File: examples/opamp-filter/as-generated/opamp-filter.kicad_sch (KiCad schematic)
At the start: 22 parts, among them J1 IN, J2 5V, J3 OUT, U1 MCP6001R, U2 MCP6001R

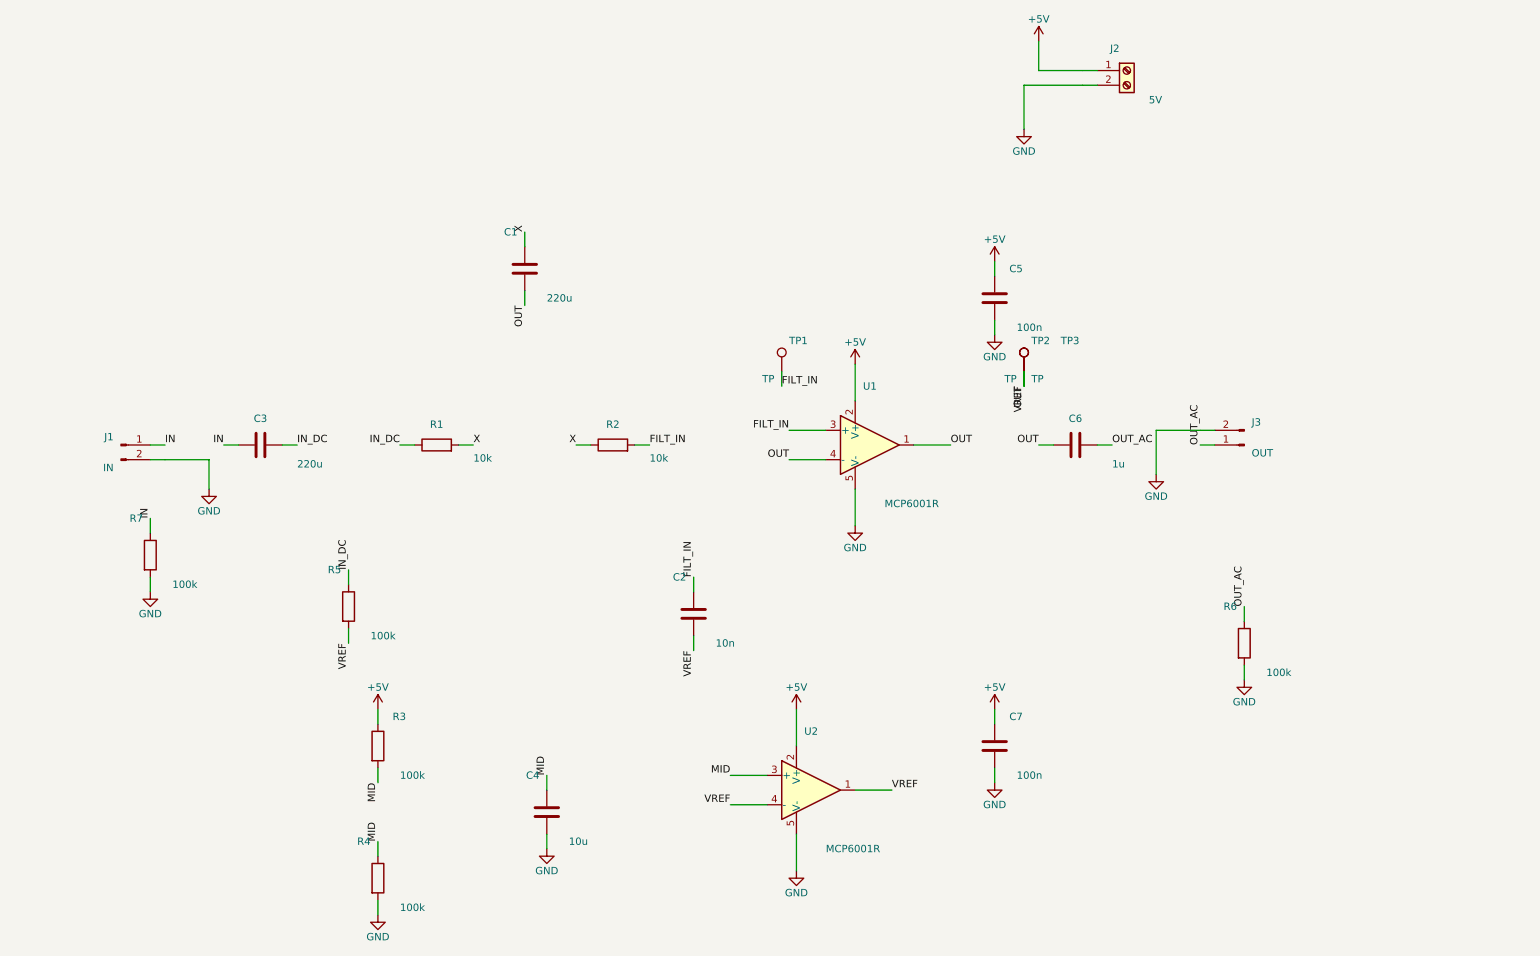
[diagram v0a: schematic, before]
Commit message: Relieve the pads, fillet the joints, and give the board its screw holes
Three of the reviewer's manufacturing points, and they largely fall out
of the one before it - once KiCad fills the plane, the thermal relief it
was already asked for in the file actually appears.

**Thermal relief.** The zones said thermal all along; our own filler
ignored it and flooded every land solid. KiCad's does not, so every
through-hole ground pad now sits in a gap bridged by four spokes and an
iron can bring the joint up without heating a hundred square millimetres
of copper. `layout.solid_pad_connection` reports the setting when a
board turns it off: drilled pads only, because a surface pad reflows in
an oven that is heating the plane anyway and flooding it is often the
better thermal answer.

**Teardrops.** A track entering a land is a step change in width, and a
step change is where copper tears - the connector gets levered on and
off, the drill wanders, and the crack starts at the corner. `_teardrops`
replaces the first stretch of each run with a three-step taper into the
land, checked against its neighbours before it is kept, so a fillet
never eats the clearance a fine-pitch escape needs. It *replaces* rather
than overlays: laying the taper on top of the run drew the same copper
twice, and `route.acute_angle` reported all thirty of them, correctly.
`route.mixed_track_widths` learns what a fillet looks like so a properly
filleted board does not read as one nobody decided the width of.

**Mounting holes.** Four M3 holes near the corners, placed before the
router runs because they are obstacles, and slid along the edges or a
little inboard where a connector body has the corner - the motor board
and the op-amp take three, which is what those floorplans have room for.
Grounded on the motor driver, whose chassis is metal and part of the
shield, plain on the rest: bonding the enclosure to the reference is the
enclosure's decision, not the board's.

Two things that fell out of placing par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
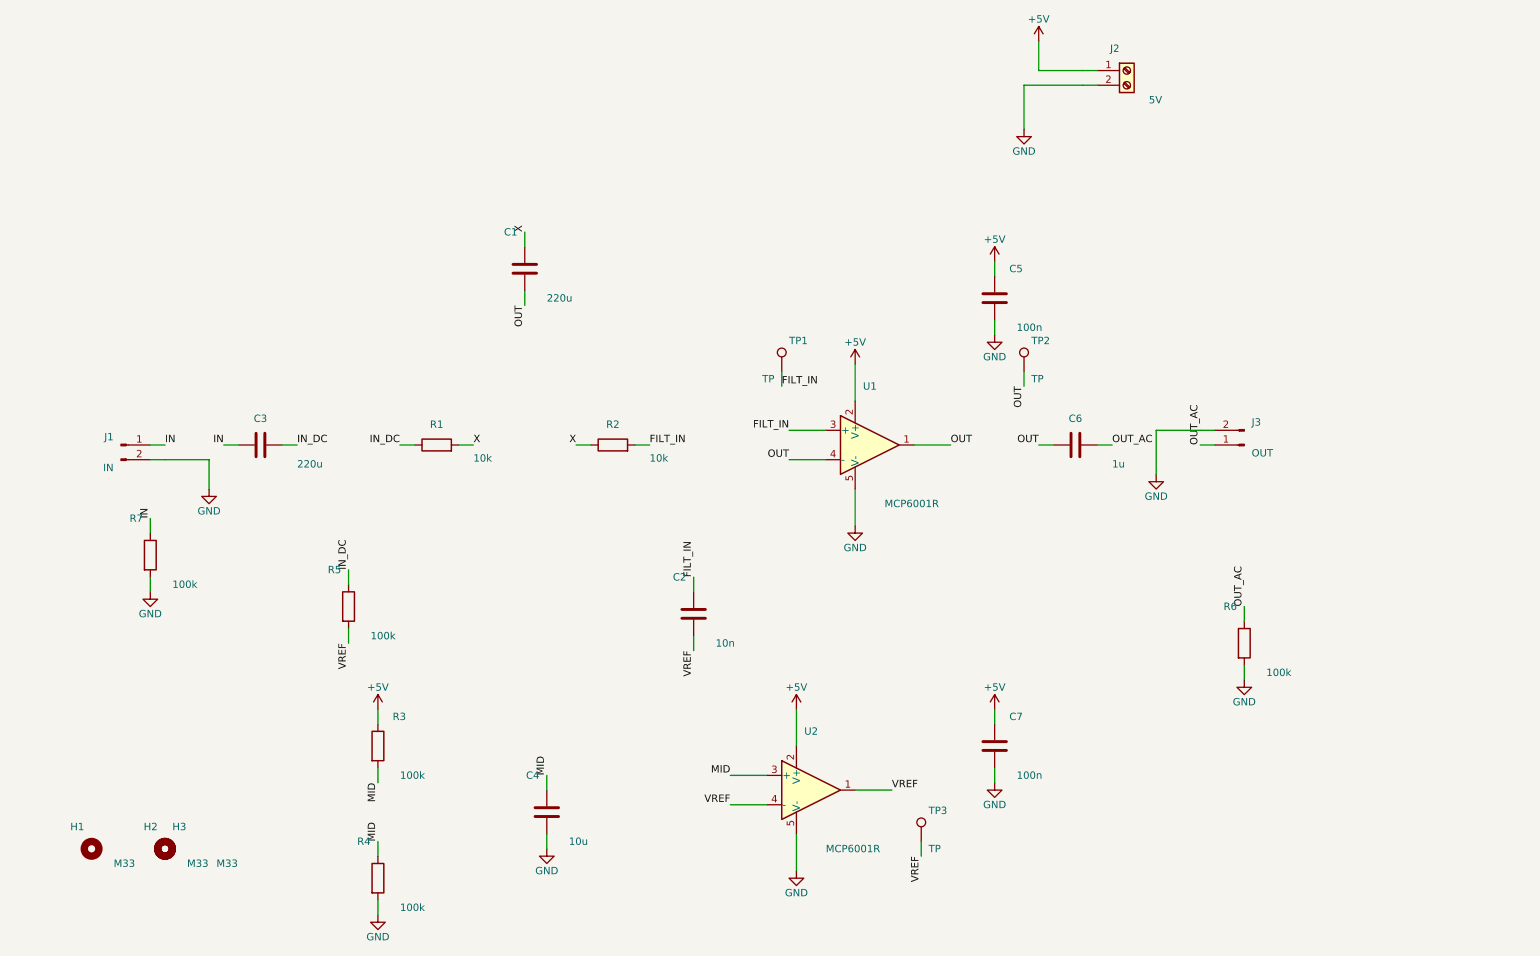
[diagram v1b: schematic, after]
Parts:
- added H1, H2, H3: M33, MountingHole:MountingHole_3.2mm_M3, symbol Mechanical:MountingHole
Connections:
- net OUT: no longer C2.2, R5.2, TP3.1, U2.1, U2.4 (-)
- new net VREF: C2.2, R5.2, TP3.1, U2.1, U2.4 (-)
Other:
- moved on the sheet: TP3
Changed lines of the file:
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@@
     (instances (project "opamp-filter" (path "/efb028ab-a5b5-5d27-b654-08a8ba6b5d9d" (reference "TP2") (unit 1))))
   )
-  (wire (pts (xy 187.0 87.44) (xy 187.0 89.98)) (stroke (width 0) (type default)))
-  (label "VREF" (at 187.0 89.98 90) (effects (font (size 1.27 1.27)) (justify right bottom)))
-  (symbol (lib_id "Connector:TestPoint") (at 187.0 87.44 0.0) (unit 1)
+  (wire (pts (xy 169.22 168.72) (xy 169.22 171.26)) (stroke (width 0) (type default)))
+  (label "VREF" (at 169.22 171.26 90) (effects (font (size 1.27 1.27)) (justify right bottom)))
+  (symbol (lib_id "Connector:TestPoint") (at 169.22 168.72 0.0) (unit 1)
     (exclude_from_sim no) (in_bom yes) (on_board yes) (dnp no)
-    (property "Reference" "TP3" (at 193.35 82.106 0) (effects (font (size 1.27 1.27)) (justify left)))
-    (property "Value" "TP" (at 185.73 88.71 0) (effects (font (size 1.27 1.27)) (justify right)))
-    (property "Footprint" "TestPoint:TestPoint_Pad_D1.5mm" (at 187.0 87.44 0) (effects (font (size 1.27 1.27)) hide))
-    (property "Datasheet" "~" (at 187.0 87.44 0) (effects (font (size 1.27 1.27)) hide))
+    (property "Reference" "TP3" (at 170.49 163.386 0) (effects (font (size 1.27 1.27)) (justify left)))
+    (property "Value" "TP" (at 170.49 169.99 0) (effects (font (size 1.27 1.27)) (justify left)))
+    (property "Footprint" "TestPoint:TestPoint_Pad_D1.5mm" (at 169.22 168.72 0) (effects (font (size 1.27 1.27)) hide))
+    (property "Datasheet" "~" (at 169.22 168.72 0) (effects (font (size 1.27 1.27)) hide))
     (pin "1" (uuid "12ecb46a-2c7d-56f1-aa85-0574999d84bc-p1"))
     (instances (project "opamp-filter" (path "/efb028ab-a5b5-5d27-b654-08a8ba6b5d9d" (reference "TP3") (unit 1))))
   )
+  (symbol (lib_id "Mechanical:MountingHole") (at 25.71 169.99 0.0) (unit 1)
+    (exclude_from_sim no) (in_bom yes) (on_board yes) (dnp no)
+    (property "Reference" "H1" (at 24.44 166.18 0) (effects (font (size 1.27 1.27)) (justify right)))
+    (property "Value" "M33" (at 29.52 172.53 0) (effects (font (size 1.27 1.27)) (justify left)))
+    (property "Footprint" "MountingHole:MountingHole_3.2mm_M3" (at 25.71 169.99 0) (effects (font (size 1.27 1.27)) hide))
+    (property "Datasheet" "~" (at 25.71 169.99 0) (effects (font (size 1.27 1.27)) hide))
+    (instances (project "opamp-filter" (path "/efb028ab-a5b5-5d27-b654-08a8ba6b5d9d" (reference "H1") (unit 1))))
+  )
+  (symbol (lib_id "Mechanical:MountingHole") (at 38.41 169.99 0.0) (unit 1)
+    (exclude_from_sim no) (in_bom yes) (on_board yes) (dnp no)
+    (property "Reference" "H2" (at 37.14 166.18 0) (effects (font (size 1.27 1.27)) (justify right)))
+    (property "Value" "M33" (at 42.22 172.53 0) (effects (font (size 1.27 1.27)) (justify left)))
+    (property "Footprint" "MountingHole:MountingHole_3.2mm_M3" (at 38.41 169.99 0) (effects (font (size 1.27 1.27)) hide))
+    (property "Datasheet" "~" (at 38.41 169.99 0) (effects (font (size 1.27 1.27)) hide))
+    (instances (project "opamp-filter" (path "/efb028ab-a5b5-5d27-b654-08a8ba6b5d9d" (reference "H2") (unit 1))))
+  )
+  (symbol (lib_id "Mechanical:MountingHole") (at 38.41 169.99 0.0) (unit 1)
+    (exclude_from_sim no) (in_bom yes) (on_board yes) (dnp no)
+    (property "Reference" "H3" (at 39.68 166.18 0) (effects (font (size 1.27 1.27)) (justify left)))
+    (property "Value" "M33" (at 47.3 172.53 0) (effects (font (size 1.27 1.27)) (justify left)))
+    (property "Footprint" "MountingHole:MountingHole_3.2mm_M3" (at 38.41 169.99 0) (effects (font (size 1.27 1.27)) hide))
+    (property "Datasheet" "~" (at 38.41 169.99 0) (effects (font (size 1.27 1.27)) hide))
+    (instances (project "opamp-filter" (path "/efb028ab-a5b5-5d27-b654-08a8ba6b5d9d" (reference "H3") (unit 1))))
+  )
   (wire (pts (xy 38.41 102.68) (xy 46.03 102.68)) (stroke (width 0) (type default)))

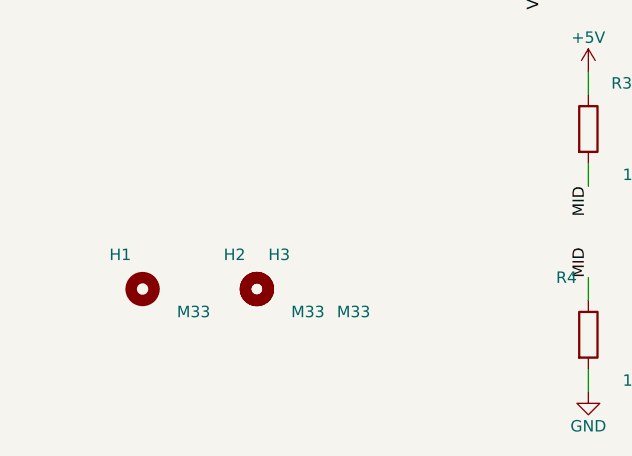
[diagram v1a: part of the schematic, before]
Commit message: Give the assembly machine something to aim at
Fiducials: three copper dots in bare mask windows, near three different
corners so a pick-and-place gets rotation as well as offset. It aligns
to the board, not to the drawing - without them it has only the routed
outline, cut to a tolerance ten times looser than the placement a 0.5 mm
pitch part is asking for. `fab.no_fiducials` reports a fine-pitch board
that has none, as context rather than as a fault: plenty of boards are
built one at a time with tweezers.

They share the corner search with the mounting holes, which is where
this found a real bug: `_courtyard_box` read lines and rectangles only,
and a mounting hole draws its courtyard as one circle - so every hole
measured as taking up no room at all, and the first three fiducials
landed on top of three screw holes. Circles and arcs count now.

Co-Authored-By: Claude Fable 5 <noreply@anthropic.com>
Claude-Session: https://claude.ai/code/session_01DUj7Ltu92tWg159mCSacwY
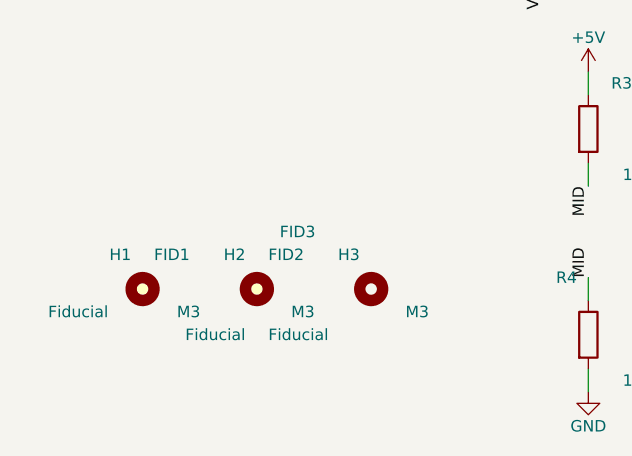
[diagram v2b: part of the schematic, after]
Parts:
- added FID1, FID2, FID3: Fiducial, Fiducial:Fiducial_1mm_Mask2mm, symbol Mechanical:Fiducial
- H1, H2, H3: value M33 -> M3
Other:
- moved on the sheet: H3
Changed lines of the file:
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@@
     (exclude_from_sim no) (in_bom yes) (on_board yes) (dnp no)
     (property "Reference" "H1" (at 24.44 166.18 0) (effects (font (size 1.27 1.27)) (justify right)))
-    (property "Value" "M33" (at 29.52 172.53 0) (effects (font (size 1.27 1.27)) (justify left)))
+    (property "Value" "M3" (at 29.52 172.53 0) (effects (font (size 1.27 1.27)) (justify left)))
     (property "Footprint" "MountingHole:MountingHole_3.2mm_M3" (at 25.71 169.99 0) (effects (font (size 1.27 1.27)) hide))
     (property "Datasheet" "~" (at 25.71 169.99 0) (effects (font (size 1.27 1.27)) hide))
@@
     (exclude_from_sim no) (in_bom yes) (on_board yes) (dnp no)
     (property "Reference" "H2" (at 37.14 166.18 0) (effects (font (size 1.27 1.27)) (justify right)))
-    (property "Value" "M33" (at 42.22 172.53 0) (effects (font (size 1.27 1.27)) (justify left)))
+    (property "Value" "M3" (at 42.22 172.53 0) (effects (font (size 1.27 1.27)) (justify left)))
     (property "Footprint" "MountingHole:MountingHole_3.2mm_M3" (at 38.41 169.99 0) (effects (font (size 1.27 1.27)) hide))
     (property "Datasheet" "~" (at 38.41 169.99 0) (effects (font (size 1.27 1.27)) hide))
     (instances (project "opamp-filter" (path "/efb028ab-a5b5-5d27-b654-08a8ba6b5d9d" (reference "H2") (unit 1))))
   )
-  (symbol (lib_id "Mechanical:MountingHole") (at 38.41 169.99 0.0) (unit 1)
+  (symbol (lib_id "Mechanical:MountingHole") (at 51.11 169.99 0.0) (unit 1)
     (exclude_from_sim no) (in_bom yes) (on_board yes) (dnp no)
-    (property "Reference" "H3" (at 39.68 166.18 0) (effects (font (size 1.27 1.27)) (justify left)))
-    (property "Value" "M33" (at 47.3 172.53 0) (effects (font (size 1.27 1.27)) (justify left)))
-    (property "Footprint" "MountingHole:MountingHole_3.2mm_M3" (at 38.41 169.99 0) (effects (font (size 1.27 1.27)) hide))
-    (property "Datasheet" "~" (at 38.41 169.99 0) (effects (font (size 1.27 1.27)) hide))
+    (property "Reference" "H3" (at 49.84 166.18 0) (effects (font (size 1.27 1.27)) (justify right)))
+    (property "Value" "M3" (at 54.92 172.53 0) (effects (font (size 1.27 1.27)) (justify left)))
+    (property "Footprint" "MountingHole:MountingHole_3.2mm_M3" (at 51.11 169.99 0) (effects (font (size 1.27 1.27)) hide))
+    (property "Datasheet" "~" (at 51.11 169.99 0) (effects (font (size 1.27 1.27)) hide))
     (instances (project "opamp-filter" (path "/efb028ab-a5b5-5d27-b654-08a8ba6b5d9d" (reference "H3") (unit 1))))
   )
+  (symbol (lib_id "Mechanical:Fiducial") (at 25.71 169.99 0.0) (unit 1)
+    (exclude_from_sim no) (in_bom yes) (on_board yes) (dnp no)
+    (property "Reference" "FID1" (at 26.98 166.18 0) (effects (font (size 1.27 1.27)) (justify left)))
+    (property "Value" "Fiducial" (at 21.9 172.53 0) (effects (font (size 1.27 1.27)) (justify right)))
+    (property "Footprint" "Fiducial:Fiducial_1mm_Mask2mm" (at 25.71 169.99 0) (effects (font (size 1.27 1.27)) hide))
+    (property "Datasheet" "~" (at 25.71 169.99 0) (effects (font (size 1.27 1.27)) hide))
+    (instances (project "opamp-filter" (path "/efb028ab-a5b5-5d27-b654-08a8ba6b5d9d" (reference "FID1") (unit 1))))
+  )
+  (symbol (lib_id "Mechanical:Fiducial") (at 38.41 169.99 0.0) (unit 1)
+    (exclude_from_sim no) (in_bom yes) (on_board yes) (dnp no)
+    (property "Reference" "FID2" (at 39.68 166.18 0) (effects (font (size 1.27 1.27)) (justify left)))
+    (property "Value" "Fiducial" (at 39.68 175.07 0) (effects (font (size 1.27 1.27)) (justify left)))
+    (property "Footprint" "Fiducial:Fiducial_1mm_Mask2mm" (at 38.41 169.99 0) (effects (font (size 1.27 1.27)) hide))
+    (property "Datasheet" "~" (at 38.41 169.99 0) (effects (font (size 1.27 1.27)) hide))
+    (instances (project "opamp-filter" (path "/efb028ab-a5b5-5d27-b654-08a8ba6b5d9d" (reference "FID2") (unit 1))))
+  )
+  (symbol (lib_id "Mechanical:Fiducial") (at 38.41 169.99 0.0) (unit 1)
+    (exclude_from_sim no) (in_bom yes) (on_board yes) (dnp no)
+    (property "Reference" "FID3" (at 40.95 163.64 0) (effects (font (size 1.27 1.27)) (justify left)))
+    (property "Value" "Fiducial" (at 37.14 175.07 0) (effects (font (size 1.27 1.27)) (justify right)))
+    (property "Footprint" "Fiducial:Fiducial_1mm_Mask2mm" (at 38.41 169.99 0) (effects (font (size 1.27 1.27)) hide))
+    (property "Datasheet" "~" (at 38.41 169.99 0) (effects (font (size 1.27 1.27)) hide))
+    (instances (project "opamp-filter" (path "/efb028ab-a5b5-5d27-b654-08a8ba6b5d9d" (reference "FID3") (unit 1))))
+  )
   (wire (pts (xy 38.41 102.68) (xy 46.03 102.68)) (stroke (width 0) (type default)))
